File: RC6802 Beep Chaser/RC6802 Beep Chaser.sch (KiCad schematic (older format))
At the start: 25 parts, among them J2 RC6802_UI_Port, M3 Mounting, M4 Mounting, U1 74LS374, U2 74LS374

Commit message: Latch beep chaser outputs on write only
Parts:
- added C3: 100nF, Capacitors_THT:C_Disc_D4.7mm_W2.5mm_P5.00mm, symbol C
- added J1: SPK, Pin_Headers:Pin_Header_Straight_1x02_Pitch2.54mm, symbol Conn_01x02
- added J3: EXT, Pin_Headers:Pin_Header_Straight_1x09_Pitch2.54mm, symbol Conn_01x09
- added J4: READ, Pin_Headers:Pin_Header_Straight_1x02_Pitch2.54mm, symbol Conn_01x02
- added U3: 74LS138, Housings_DIP:DIP-16_W7.62mm_Socket, symbol 74LS138
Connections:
- net D1: now also U2.4 (D1)
- net D2: now also U2.7 (D2)
- net D3: now also U2.8 (D3)
- net D4: now also U2.13 (D4)
- net D5: now also U2.14 (D5)
- net D6: now also U2.17 (D6)
- net D7: now also U2.18 (D7)
- net GND: now also C3.2, J1.2 (Pin_2), J3.9 (Pin_9), U3.4 (E1), U3.5 (E2), U3.8 (GND); no longer U2.13 (D4), U2.14 (D5), U2.17 (D6), U2.18 (D7), U2.4 (D1), U2.7 (D2), U2.8 (D3)
- net IO1: now also U3.1 (A0); no longer U1.11 (Cp)
- net IO2: now also U3.2 (A1); no longer U2.11 (Cp)
- net VCC: now also C3.1, J3.1 (Pin_1), U3.16 (VCC), U3.6 (E3)
- net R/~W: now reaches J2.19 (P19)
- net R/~W: now also U3.3 (A2)
- net at LS1.1, R1.1: now also J1.1 (Pin_1)
- net at U2.12 (O4): now also J3.5 (Pin_5)
- net at U2.15 (O5): now also J3.6 (Pin_6)
- net at U2.16 (O6): now also J3.7 (Pin_7)
- net at U2.19 (O7): now also J3.8 (Pin_8)
- net at U2.5 (O1): now also J3.2 (Pin_2)
- net at U2.6 (O2): now also J3.3 (Pin_3)
- net at U2.9 (O3): now also J3.4 (Pin_4)
- new net IO1_R: J4.1 (Pin_1), U3.9 (O6)
- new net IO1_W: U1.11 (Cp), U3.13 (O2)
- new net IO2_R: J4.2 (Pin_2), U3.10 (O5)
- new net IO2_W: U2.11 (Cp), U3.14 (O1)
- no-connect marks 34 -> 30
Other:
- moved on the sheet: C1, C2, D0, D1, D2, D3, D4, D5, D6, D7, J2, LS1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

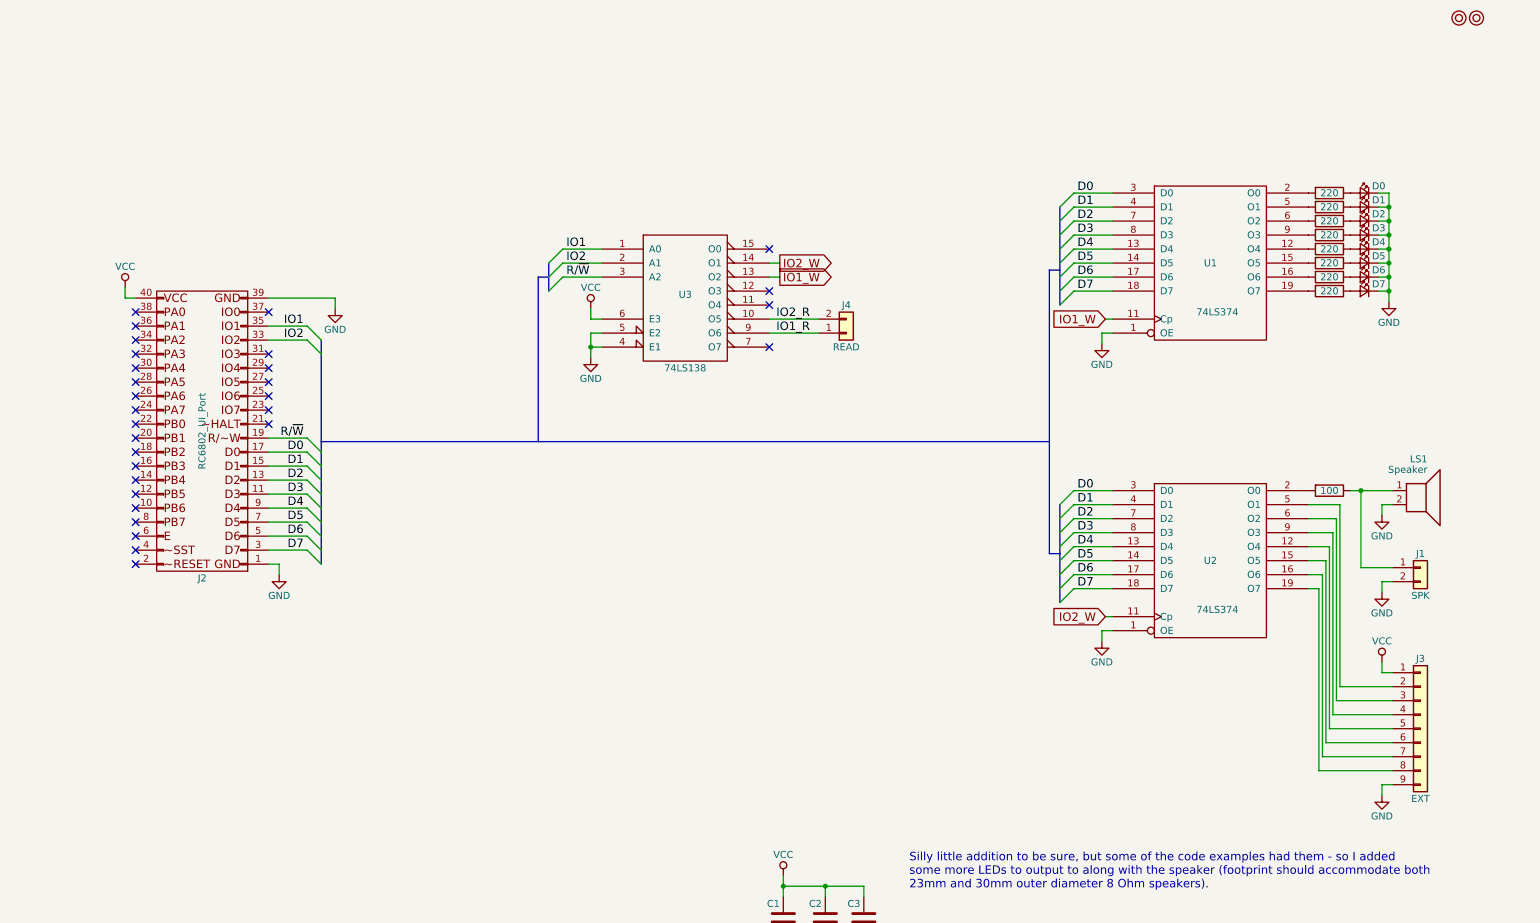
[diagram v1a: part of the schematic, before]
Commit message: Added transistor to drive speaker
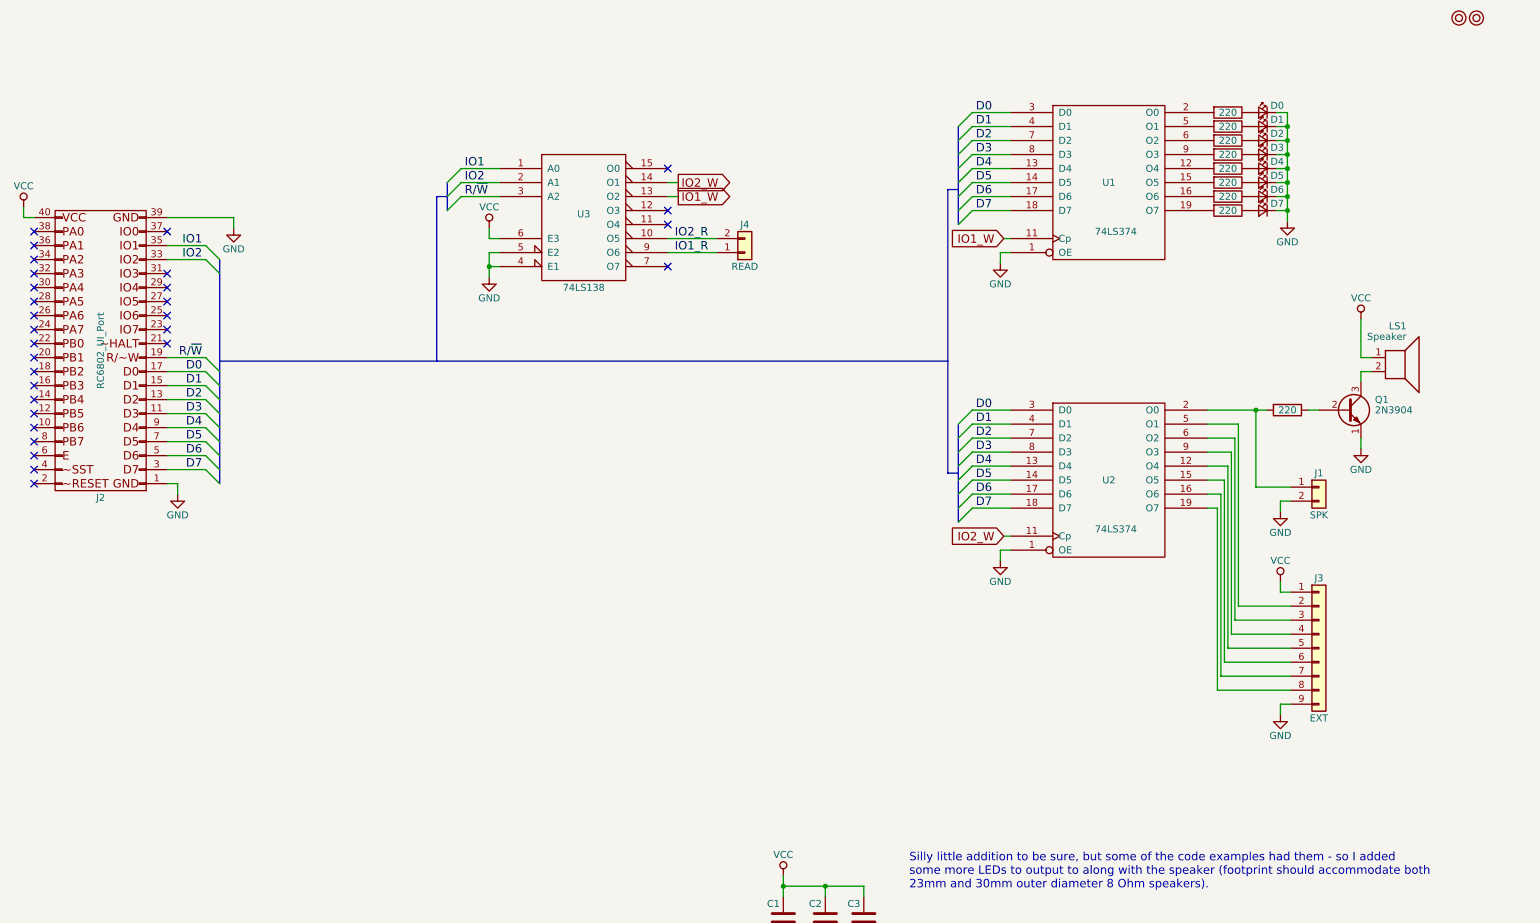
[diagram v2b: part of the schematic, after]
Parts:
- added Q1: 2N3904, TO_SOT_Packages_THT:TO-92_Inline_Wide, symbol 2N3904
- R1: value 100 -> 220
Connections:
- net GND: now also Q1.1 (E); no longer LS1.2
- net VCC: now also LS1.1
- net at R1.2, U2.2 (O0): now also J1.1 (Pin_1)
- new net: LS1.2, Q1.3 (C)
- new net: Q1.2 (B), R1.1
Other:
- moved on the sheet: D0, D1, D2, D3, D4, D5, D6, D7, J1, J2, J3, J4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
